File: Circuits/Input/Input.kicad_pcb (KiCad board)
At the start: 2 copper layers, 28.9 x 68.9 mm, 6 parts, among them P1 WRITER-VCC, SW1 MKA-10110, U1 TWE_LITE_SMD

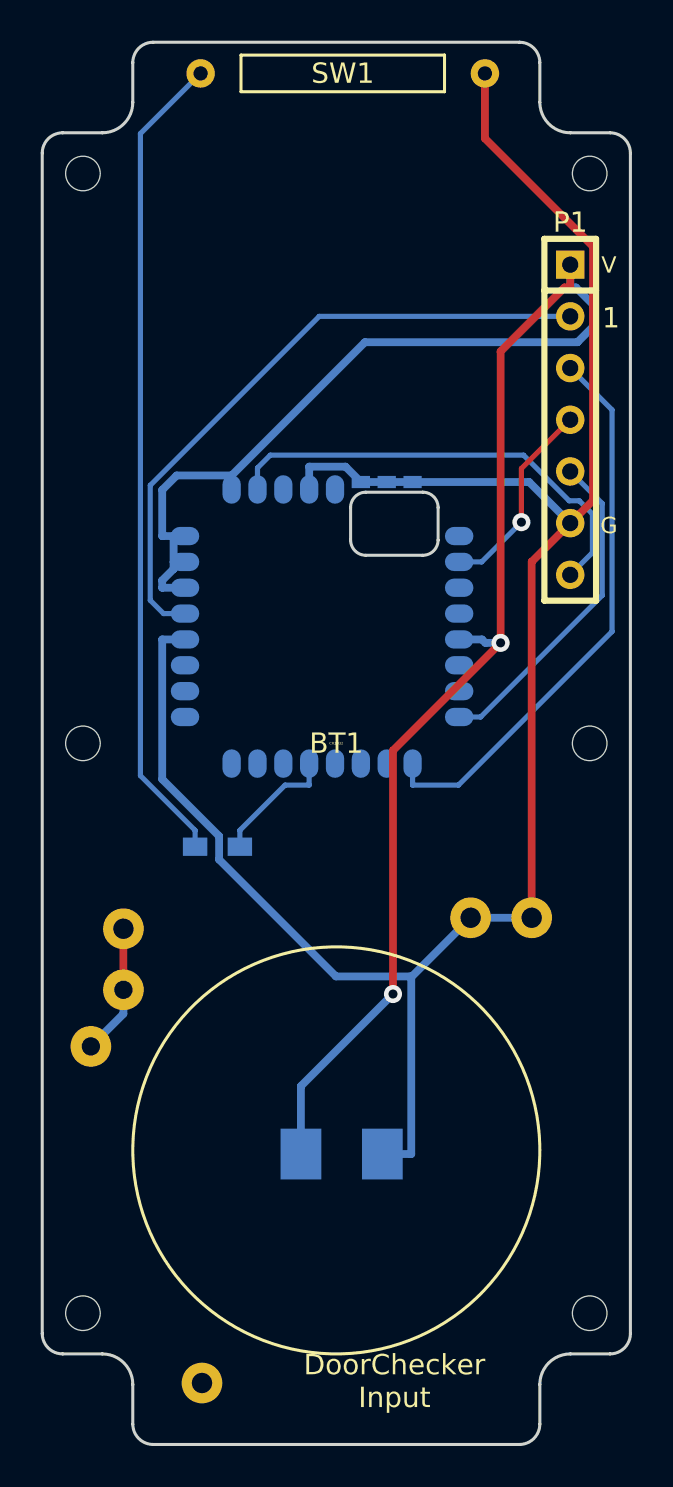
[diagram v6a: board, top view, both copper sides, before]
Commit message: Migrating to KiCad 5.0
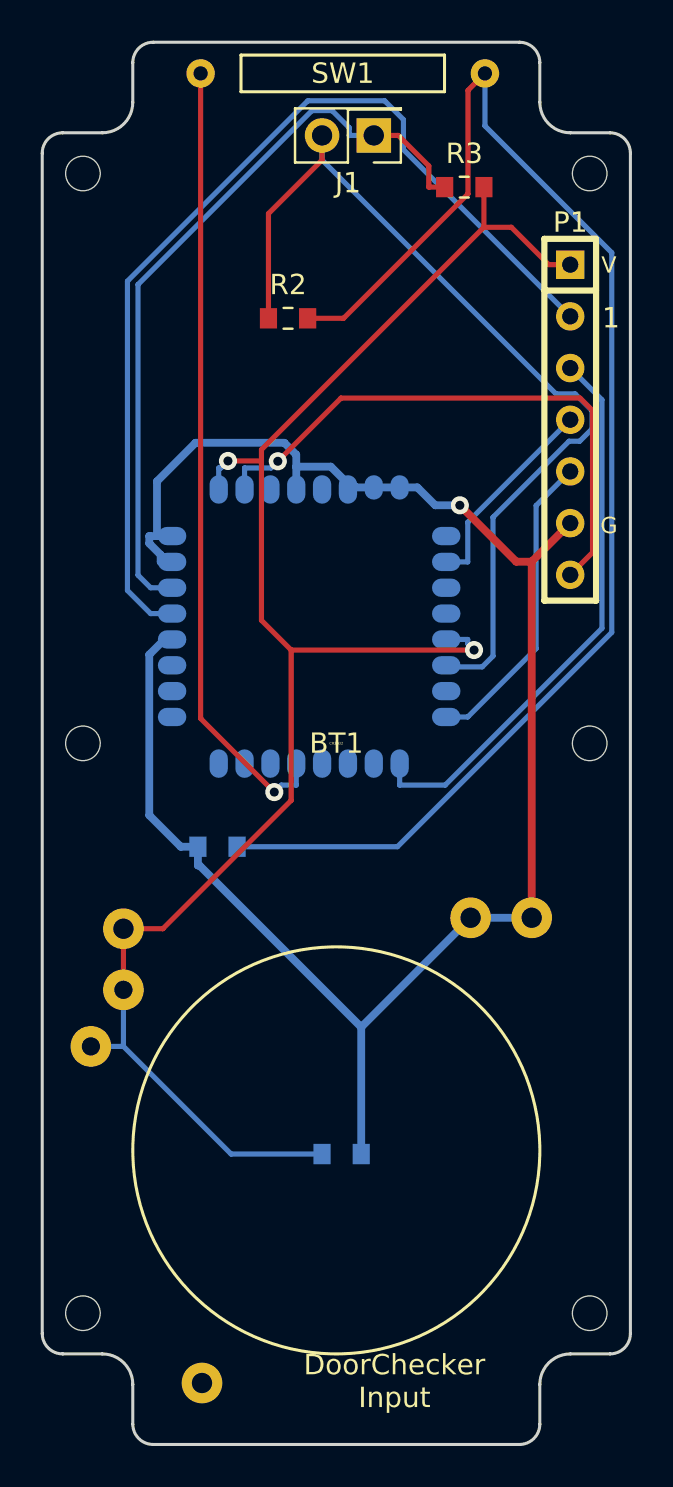
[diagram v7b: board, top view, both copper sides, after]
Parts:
- added J1: sensor, Connector_PinHeader_2.54mm:PinHeader_2x01_P2.54mm_Vertical, F.Cu at (30.5, 19.1)
- added R2: 100k, Resistor_SMD:R_0603_1608Metric_Pad0.84x1.00mm_HandSolder, F.Cu at (26.3, 28.0)
- added R3: 100k, Resistor_SMD:R_0603_1608Metric_Pad0.84x1.00mm_HandSolder, F.Cu at (34.9, 21.6)
- C1: value 100u -> 1uF; footprint Capacitors_SMD:C_1210_HandSoldering -> Capacitor_SMD:C_0603_1608Metric_Pad0.84x1.00mm_HandSolder
- R1: footprint Resistors_SMD:R_0603_HandSoldering -> Resistor_SMD:R_0603_1608Metric_Pad0.84x1.00mm_HandSolder
- U1: value TWE_LITE_SMD -> TWELITE_SMD; footprint favorites:TWE-001L-NC7 -> RF_Module:TWELITE_SMD
- moved U1 0.64 mm to (27.3, 43.2)
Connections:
- net /DO1 renamed Net-(U1-Pad3)
- BT1 pad 1: /DC3V -> /Vcc
- C1 pad 1: VCC -> /Vcc
- P1 pad 0: VCC -> /Vcc
- R1 pad 1: /DI1 -> Net-(R1-Pad1)
- R1 pad 2: Net-(R1-Pad2) -> GND
- SW1 pad 1: GND -> Net-(R1-Pad1)
- SW1 pad 2: Net-(R1-Pad2) -> /DI1
- U1 pad 22: VCC -> Net-(J1-Pad1)
- U1 pad 23: VCC -> GND
- U1 pad 24: VCC -> GND
- U1 pad 25: VCC -> /Vcc
- U1 pad 5: VCC -> /Vcc
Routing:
- net VCC: track 88.1 -> 0.00 mm, vias 2 -> 0
- net /Vcc: track 0.00 -> 84.4 mm, vias 0 -> 2
- net Net-(R1-Pad1): track 0.00 -> 69.5 mm
- net Net-(J1-Pad2): track 0.00 -> 46.6 mm
- net Net-(R1-Pad2): track 40.3 -> 0.00 mm
- net Net-(J1-Pad1): track 0.00 -> 37.2 mm
- net /DI1: track 6.19 -> 39.1 mm, vias 0 -> 1
- net /RST: track 31.7 -> 48.5 mm
- net GND: track 102.2 -> 90.8 mm, vias 0 -> 1
- net /DC3V: track 6.44 -> 0.00 mm
- net /CFG: track 22.4 -> 28.4 mm, vias 0 -> 1
- net /TXD: track 16.2 -> 15.2 mm
- net /PRG: track 9.89 -> 10.1 mm, vias 1 -> 0

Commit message: Updated footprint
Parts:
- U1: footprint RF_Module:TWELITE_SMD -> RF_Module:TWE-L-W7
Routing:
- net GND: track 90.8 -> 142.6 mm, vias 1 -> 0
- net Net-(J1-Pad2): track 46.6 -> 33.9 mm, vias 0 -> 1
- net /Vcc: track 84.4 -> 95.0 mm, vias 2 -> 1
- net /RST: track 48.5 -> 41.9 mm, vias 0 -> 1
- net /CFG: track 28.4 -> 23.0 mm, vias 1 -> 0
- net Net-(J1-Pad1): track 37.2 -> 33.5 mm
- net /DI1: track 39.1 -> 40.7 mm
- net /TXD: track 15.2 -> 16.5 mm
- net /PRG: vias 0 -> 1
